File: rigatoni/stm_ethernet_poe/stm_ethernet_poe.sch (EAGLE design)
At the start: 81 parts, among them J3 ARJM11C7-104-AB-EW2, U1 AZ1117EH-3.3TRG1, U2 IFX91041, U3 W5500, U4 TPS26600PWPR, X1 25MHz

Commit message: work underway
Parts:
- removed C10: 4.7uF, rcl:C-USC0603
- removed C11, C24, C25: 10000pF, adafruit:C-USC0402
- removed C12, C14, C20, C7, C9: 0.1uF, adafruit:C-USC0402
- removed C13, C23: 0.220uF, rcl:C-USC0603
- removed C15: 100uF, rcl:CPOL-USE2-5
- removed C18: 22uF, rcl:C-USC0603
- removed C19: 10000pF, 50V, rcl:C-USC0603
- removed C22: 10000pF, rcl:C-USC0603
- removed C29: 22uF, SparkFun-Capacitors:22UF-POLAR-PANASONIC_C-35V-20%
- removed C30: 1uF, 50V, rcl:C-USC0603
- removed C31: 100uF, 35V, rcl:CPOL-USE2.5-7
- removed D1: NTS260ESFT3G, ethernet_poe:NTS260ESFT3G
- removed F1: 1A (Trip), ethernet_poe:0ZCG0050AF2C
- removed H1, H2: MOUNT-PAD-ROUND2.8, holes:MOUNT-PAD-ROUND2.8
- removed J1: (no value), SparkFun-Connectors:CONN_05
- removed J2: (no value), SparkFun-Connectors:CONN_07
- removed L1: 47uH, ethernet_poe_v2.1:7447709470_7447709470
- removed R26: 10k, rcl:R-US_R0603
- removed R27: 715k, 1%, rcl:R-US_R0603
- removed U3: W5500, ethernet_poe:W5500
- removed U4: TPS26600PWPR, ethernet_poe:TPS26600PWPR
- C1: value 0.022uF, 50V -> 1000pF; device rcl:C-USC0603 -> adafruit:C-USC0603
- C2: value 18pF -> 1uF; device rcl:C-USC0603 -> adafruit:C-USC0603
- C26: value 10000pF -> 1000pF
- C28: value 0.1uF -> 10uF
- C3: value 2.2uF, 50V -> 0.1uF; device rcl:C-USC0603 -> adafruit:C-USC0603
- C4: device adafruit:C-USC0402 -> adafruit:C-USC0603
- C5: value 0.1uF -> 16pF; device adafruit:C-USC0402 -> resistor:C-USC0603
- C6: value 18pF -> 16pF; device rcl:C-USC0603 -> resistor:C-USC0603
- R1: value 22k -> 49.9, 1%; device rcl:R-US_R0603 -> adafruit:R-US_R0402
- R11: value 66.5k, 1% -> 33; device rcl:R-US_R0603 -> adafruit:R-US_R0402
- R12: value 11.8k, 1% -> 33; device rcl:R-US_R0603 -> adafruit:R-US_R0402
- R13: value 30.1k, 1% -> 10k; device rcl:R-US_R0603 -> adafruit:R-US_R0402
- R14: value 20k, 1% -> 10k; device rcl:R-US_R0603 -> adafruit:R-US_R0402
- R15, R25, R5: device rcl:R-US_R0603 -> adafruit:R-US_R0402
- R16: value 10k -> 1k; device rcl:R-US_R0603 -> adafruit:R-US_R0402
- R2: value 1M -> 49.9, 1%
- R4: value 12.4k, 1% -> 12.1k; device rcl:R-US_R0603 -> adafruit:R-US_R0402
- R6, R7: value 10k -> 33; device rcl:R-US_R0603 -> adafruit:R-US_R0402
- U2: value IFX91041 -> LAN8742A; device ethernet_poe:IFX91041 -> RoboRacing_STM:LAN8742A
- X1: value 25MHz -> FL2500316Z; device ethernet_poe_v2.1:ABM10W-25.0000MHZ-6-K1Z-T3 -> RoboJackets-FreqGen:XTAL-3.2X2.5
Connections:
- removed net !INT: J2.1, R16.2, U3.!INTN
- removed net !SCS: J2.5, R15.2, U3.!SCSN
- removed net +5V_PREFUSE: C15.+, C23.1, F1.1, L1.2, U2.FB
- removed net 24_LOAD: J2.7, R11.1, U4.IMON
- removed net 5V_RAW: C13.2, D1.1, L1.1, U2.BUO
- removed net MISO: J2.3, U3.MISO
- removed net MOSI: J2.2, U3.MOSI
- removed net N$13: C2.1, R2.2, U3.XI, X1.IN
- removed net N$16: C1.2, R1.1
- removed net N$17: C1.1, U2.COMP
- removed net N$18: C11.1, U3.1V2O
- removed net N$19: C10.1, U3.TOCAP
- removed net N$21: R4.2, U3.EXRES1
- removed net N$27: R13.1, R14.2, U4.OVP
- removed net N$28: C3.1, U4.DVDT
- removed net N$33: R12.1, U4.ILIM
- removed net N$5: R6.1, U3.PMODE1
- removed net N$7: R7.1, U3.PMODE2
- removed net RTN: C3.2, R11.2, R12.2, R13.2, U4.MODE, U4.PAD, U4.RTN
- removed net RX_FILTER: C22.1, R25.2, R26.2
- removed net RX_N: C25.1, R26.1, U3.RXN
- removed net RX_P: C24.1, R25.1, U3.RXP
- removed net SCLK: J2.4, U3.SCLK
- new net N$1: R4.2, U2.RBIAS
- new net N$14: R12.2, R14.1, U2.CRS_DV
- new net N$2: C1.1, C2.1, U2.VDDCR
- new net RMII_CRS_DV: R12.1
- new net RMII_MDC: U2.MDC
- new net RMII_MDIO: R16.1, U2.MDIO
- new net RMII_REF_CLK: R11.1
- new net RMII_RXD0: R7.1
- new net RMII_RXD1: R6.1
- new net RMII_TXD0: U2.TXD0
- new net RMII_TXD1: U2.TXD1
- new net RMII_TX_EN: U2.TXEN
- new net XTAL1: C6.1, U2.XTAL2, X1.1
- new net XTAL2: C5.1, U2.XTAL1/CLKIN, X1.2
- net !RST: now also U2.!RST; no longer J1.2, U3.!RSTN
- net +24V: no longer C30.1, R27.1, U4.!SHDN, U4.IN
- net +24V_FUSE: no longer C19.1, C31.+, J1.1, U2.EN, U2.VS, U4.OUT
- net +3V3_A: now also R1.1, R2.2; no longer C12.1, C14.1, C29.+, C4.1, C5.1, C7.1, C9.1, U3.AVDD
- net +3V3_D: now also C3.1, C4.1, R13.2, R14.2, R15.2, R16.2, R25.2, U2.VDD1A, U2.VDD2A, U2.VDDIO; no longer C18.1, C20.1, J1.4, R15.1, R16.1, R21.1, R22.1, R5.2, R6.2, R7.2, U3.VDD
- net +5V: no longer F1.2, J1.3
- net ACTLED: no longer U3.ACTLED
- net AGND: no longer H1.MOUNT, H2.MOUNT
- net DUPLED: no longer U3.DUPLED
- net GND: now also C1.2, C3.2, R21.1, R22.1, R5.1; no longer C10.2, C11.2, C12.2, C14.2, C15.-, C18.2, C19.2, C20.2, C22.2, C23.2, C29.-, C30.2, C31.-, C7.2, C9.2, D1.2, J1.5, J2.6, R1.2, U2.SYNC, U3.AGND, U3.GND, U4.GND, X1.SHD1, X1.SHD2
- net G_LED+: now also J3.G_LED-; no longer J3.G_LED+
- net LINKLED: now also J3.G_LED+, U2.LED2; no longer J3.G_LED-, U3.LINKLED
- net N$11: now also R15.1, R7.2, U2.RXD0; no longer C6.1, R2.1, U3.XO, X1.OUT
- net N$15: now also R11.2, R25.1, U2.!INT; no longer C13.1, U2.BDS
- net N$4: now also R5.2, U2.RXER; no longer R5.1, U3.PMODE0
- net N$9: now also R13.1, R6.2, U2.RXD1; no longer R14.1, R27.2, U4.UVLO
- net RD_N: now also R2.1, U2.RXN; no longer C25.2
- net RD_P: now also R1.2, U2.RXP; no longer C24.2
- net SPDLED: now also J3.Y_LED+, U2.LED1; no longer J3.Y_LED-, U3.SPDLED
- net TX_N: now also U2.TXN; no longer U3.TXN
- net TX_P: now also U2.TXP; no longer U3.TXP
- net Y_LED+: now also J3.Y_LED-; no longer J3.Y_LED+
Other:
- note added: "Jack Chassis Ground"
- note removed: "!FLT left floating"
- note removed: "#3 (or M2.5) Drill Size"
- note removed: "1.8A Rated"
- note removed: "24V to 5V"
- note removed: "Chassis Ground"
- note removed: "Control"
- note removed: "Fuse"
- note removed: "Headers"
- note removed: "L_out = ((V_in - V_out) * V_out)/ (I_rip * f_s * V_in) 42.7uF = ((24-5)*5)/(0.25*370000*24) I_sat > 3.5A"
- note removed: "Mounting Holes"
- note removed: "Power (24V-5V)"
- note removed: "R(ILIM) = 12 / ILIM ILIM = 1 A"
- note removed: "R30, R31, R32 Configure OverV, UnderV"
- note removed: "R34 = V(IMONmax)/(I(ILIM)*75*10^-6) V(IMONmax) = max ADC voltage = 5V"
- note removed: "Undervoltage = 18V Overvoltage = 30V Current Limit = 1A"
- note removed: "V(ovpr)= R32/(R30+R31+R32) * V(ov)"
- note removed: "V(uvpr)= R31+R32/(R30+R31+R32) *V(uv)"
- moved on the sheet: C1, C2, C3, C4, C5, C6, R1, R11, R12, R13, R14, R15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

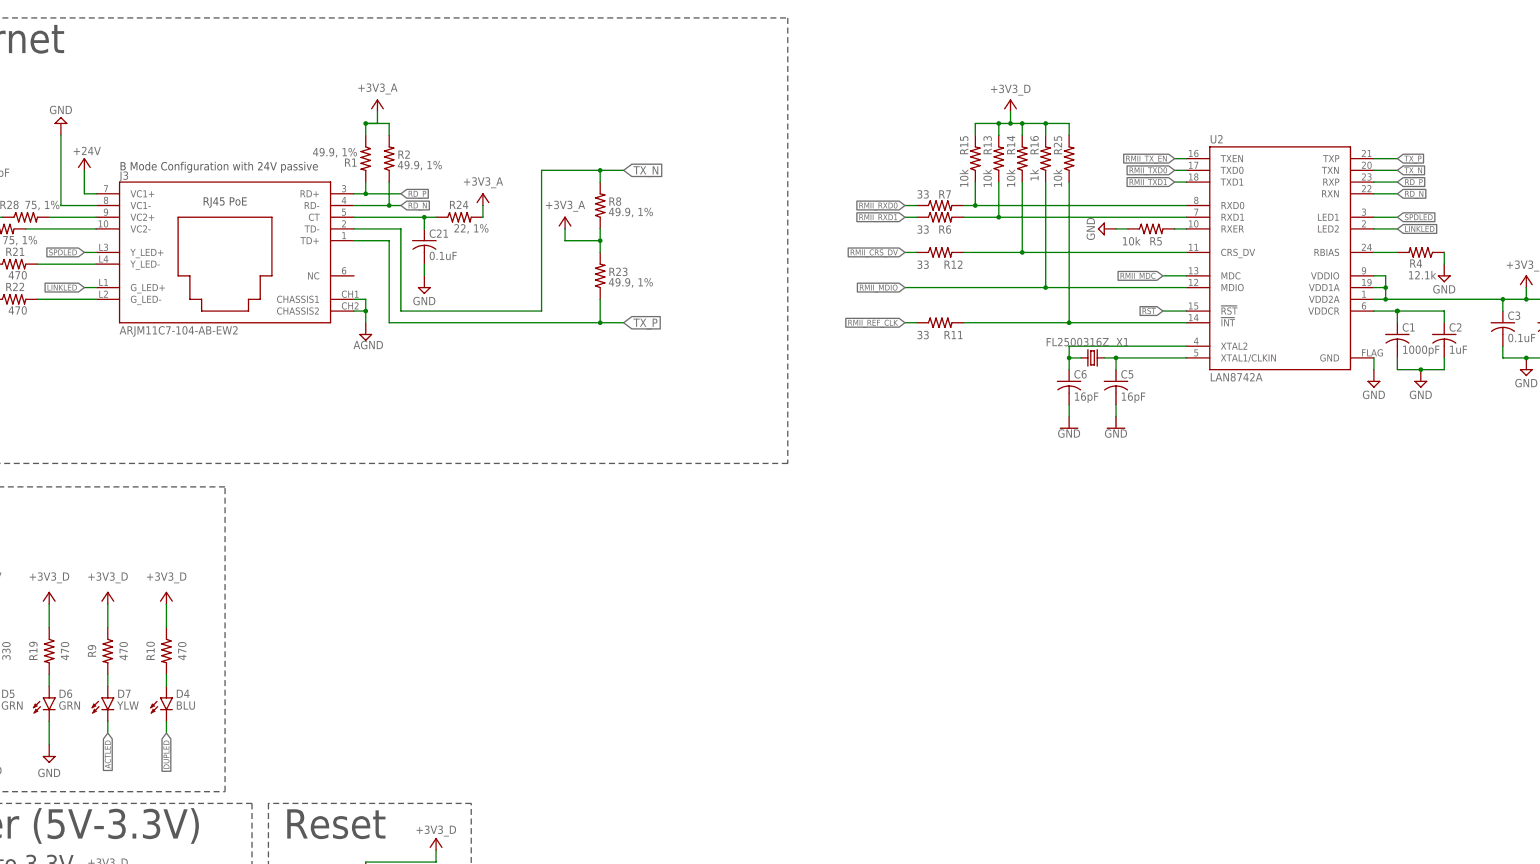
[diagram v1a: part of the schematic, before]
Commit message: with headers and TVS
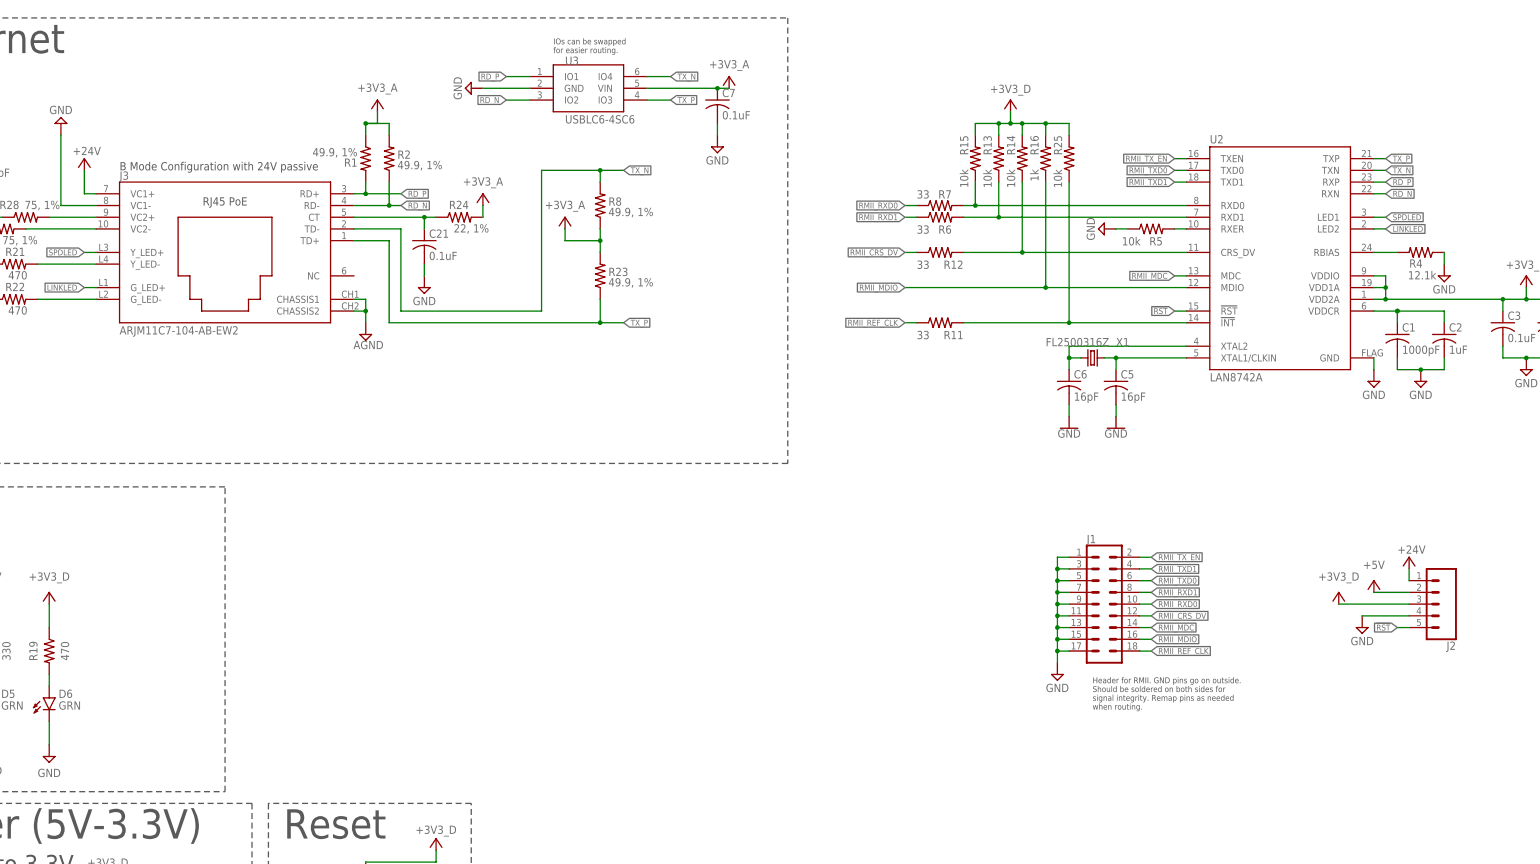
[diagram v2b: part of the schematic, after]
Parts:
- removed D4: BLU, led:LEDCHIP-LED0603
- removed D7: YLW, led:LEDCHIP-LED0603
- removed R10, R9: 470, rcl:R-US_R0603
- added C7: 0.1uF, adafruit:C-USC0402
- added J1: (no value), ethernet_poe_stm_v1.0:CONN_9X2
- added J2: (no value), SparkFun-Connectors:CONN_05
- added U3: USBLC6-4SC6, ethernet_poe_stm_v1.0:USBLC6-4SC6
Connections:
- removed net 3V3_LED1: D7.A, R9.2
- removed net 3V3_LED2: D4.A, R10.2
- removed net ACTLED: D7.C
- removed net DUPLED: D4.C
- net !RST: now also J2.5
- net +24V: now also J2.1
- net +3V3_A: now also C7.1, U3.VIN
- net +3V3_D: now also J2.3; no longer R10.1, R9.1
- net +5V: now also J2.2
- net GND: now also C7.2, J1.1, J1.11, J1.13, J1.15, J1.17, J1.3, J1.5, J1.7, J1.9, J2.4, U3.GND
- net RD_N: now also U3.IO2
- net RD_P: now also U3.IO1
- net RMII_CRS_DV: now also J1.12
- net RMII_MDC: now also J1.14
- net RMII_MDIO: now also J1.16
- net RMII_REF_CLK: now also J1.18
- net RMII_RXD0: now also J1.10
- net RMII_RXD1: now also J1.8
- net RMII_TXD0: now also J1.6
- net RMII_TXD1: now also J1.4
- net RMII_TX_EN: now also J1.2
- net TX_N: now also U3.IO4
- net TX_P: now also U3.IO3
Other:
- note added: "Header for RMII. GND pins go on outside. Should be soldered on both sides for signal integrity. Remap pins as needed when routing."
- note added: "IOs can be swapped for easier routing."
